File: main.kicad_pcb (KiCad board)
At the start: 2 copper layers, 160 x 100 mm, 95 parts, among them J1 Screw_Terminal_01x10, J2 Screw_Terminal_01x02, J3 Conn_01x03, Q1 IRF540N, Q2 IRF540N, Q3 IRF540N, Q4 IRF540N, Q5 IRF540N, SW2 Switch_All, SW3 Switch1, SW4 Switch2, SW5 Switch3, SW6 Switch4, SW7 Switch5, U1 L7805, U2 ATmega328P-PU, U3 PC817, U4 PC817, U5 PC817, U6 PC817, U7 PC817, Y1 16mHz

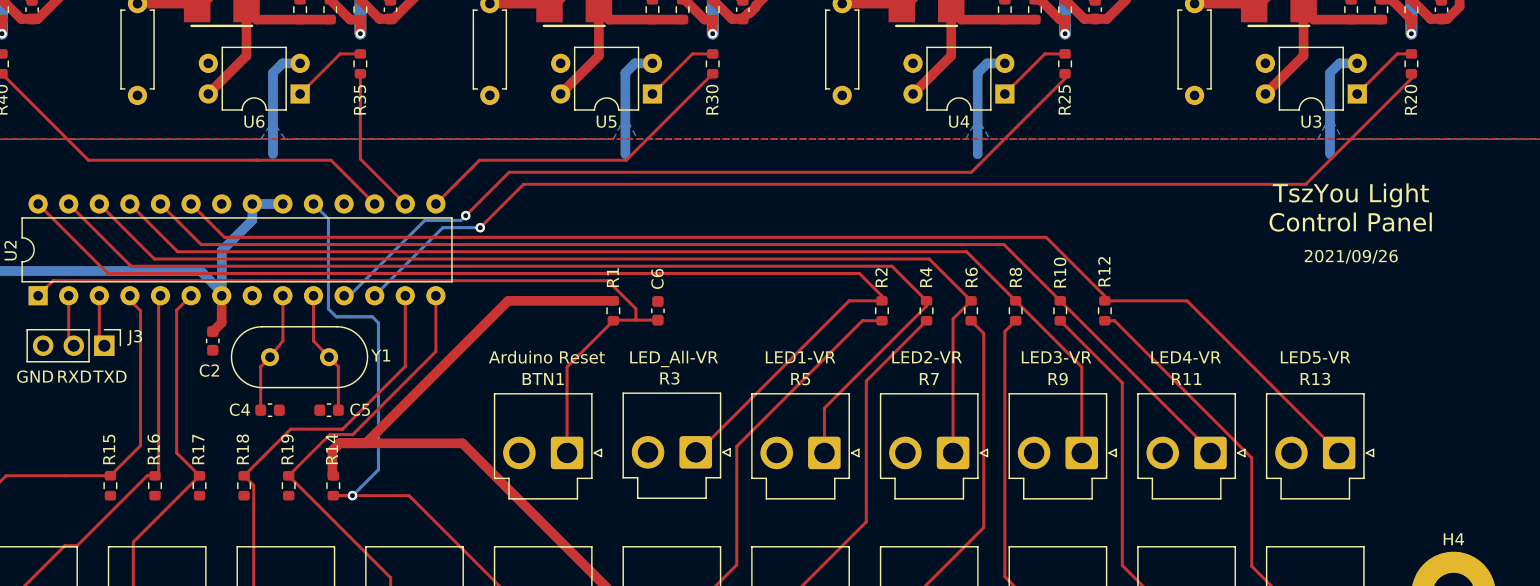
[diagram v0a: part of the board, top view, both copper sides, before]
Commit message: add arduino debug connector
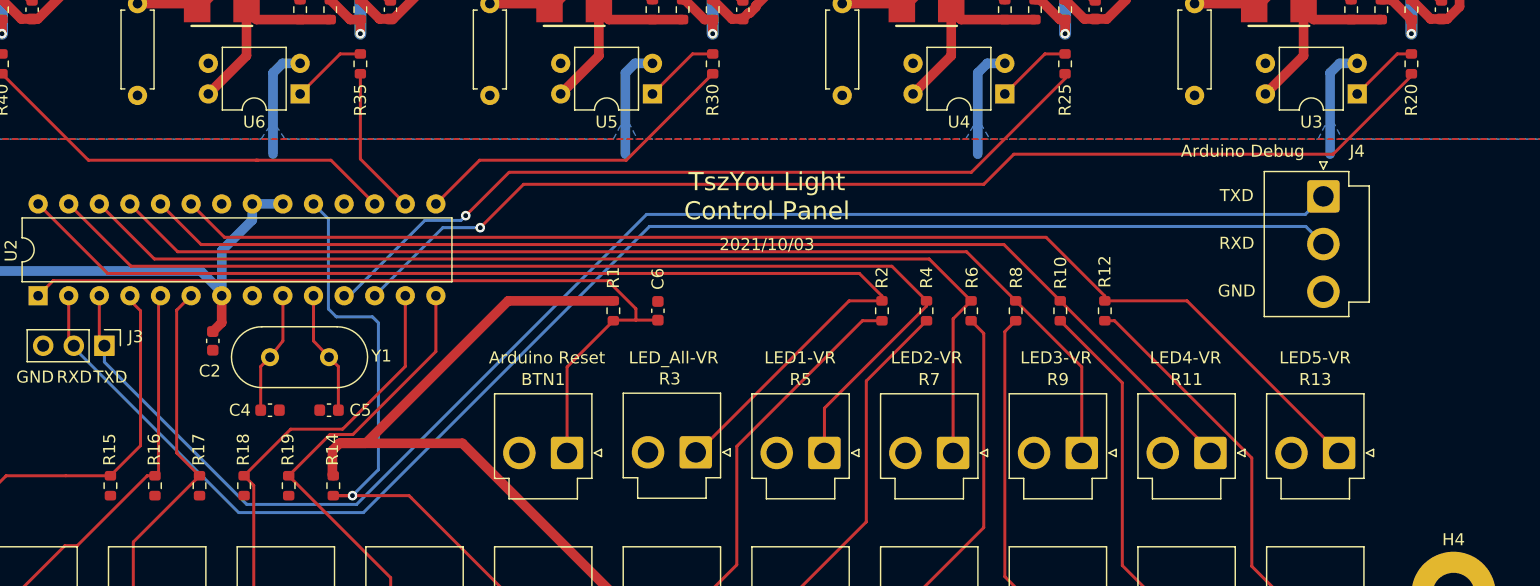
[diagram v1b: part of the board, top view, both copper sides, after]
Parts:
- added J4: Conn_01x03, local_footprint:JST_VH_B3P-VH_1x03_P3.96mm_Vertical, F.Cu at (189.2, 107.0)
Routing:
- net /RXD: track 4.32 -> 124.3 mm
- net /TXD: track 4.32 -> 122.4 mm
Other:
- board text added: "2021/10/03"
- board text added: "Arduino Debug"
- board text removed: "2021/09/26"

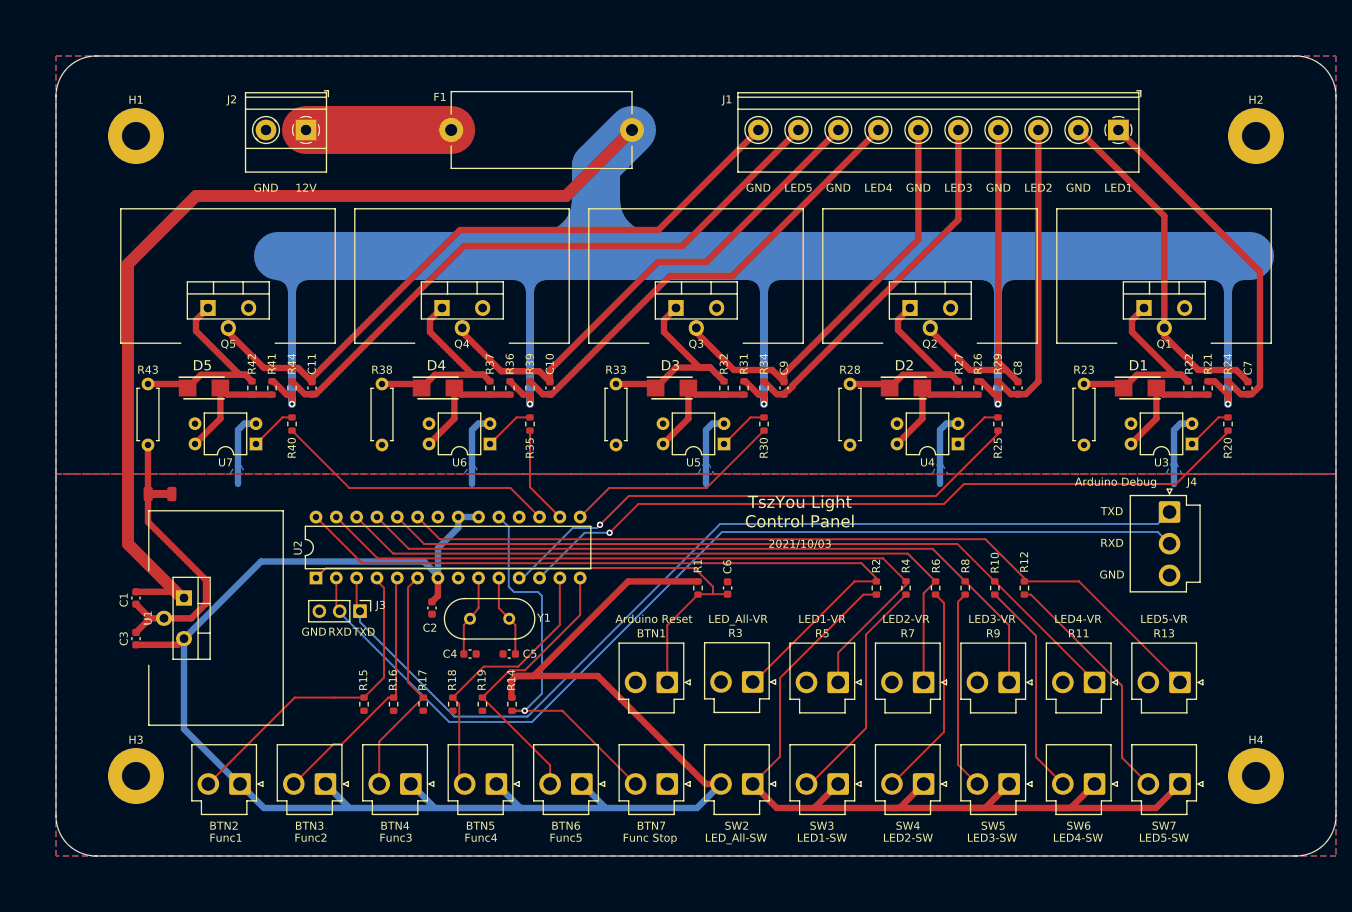
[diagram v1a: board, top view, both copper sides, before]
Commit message: [layout] modify MountingHole size and footprint
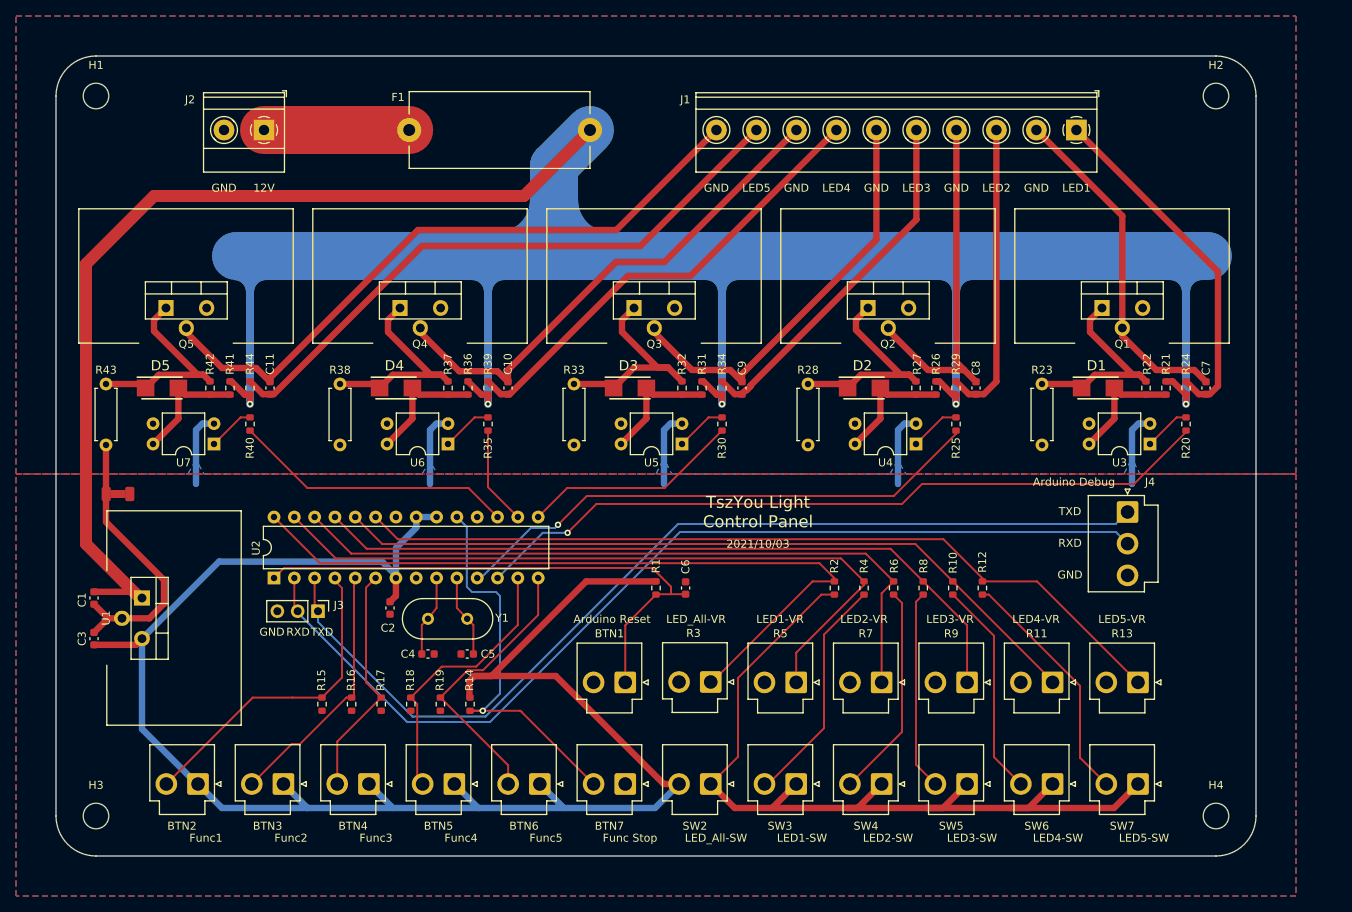
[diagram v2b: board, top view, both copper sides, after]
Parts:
- H1, H2, H3, H4: footprint MountingHole:MountingHole_3.5mm_Pad -> MountingHole:MountingHole_3.2mm_M3_ISO7380
- moved H1 7.07 mm to (55.0, 55.0)
- moved H2 7.07 mm to (195.0, 55.0)
- moved H3 7.07 mm to (55.0, 145.0)
- moved H4 7.07 mm to (195.0, 145.0)
- moved BTN1 5.25 mm to (121.2, 128.3)
- moved BTN2 5.25 mm to (67.8, 141.0)
- moved BTN3 5.25 mm to (78.4, 141.0)
- moved BTN4 5.25 mm to (89.1, 141.0)
- moved BTN5 5.25 mm to (99.8, 141.0)
- moved BTN6 5.25 mm to (110.5, 141.0)
- moved BTN7 5.25 mm to (121.2, 141.0)
- moved C1 5.25 mm to (54.8, 117.8)
- moved C10 5.25 mm to (106.5, 91.5)
- moved C11 5.25 mm to (76.8, 91.5)
- moved C2 5.25 mm to (91.8, 119.0)
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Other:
- board size 160 x 100 mm -> 150 x 100 mm
